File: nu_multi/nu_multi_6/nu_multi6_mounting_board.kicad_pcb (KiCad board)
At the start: 2 copper layers, 70 x 18.2 mm, 8 parts, among them J13 CONN_01X14, U1 nu_capsule, U2 nu_capsule, U3 nu_capsule, U4 nu_capsule, U5 nu_capsule, U6 nu_capsule

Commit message: Use 1x7p connector from cycfi lib
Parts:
- J13: footprint Pin_Headers:Pin_Header_Straight_2x07_Pitch1.00mm_SMD -> cycfi_library:pin_header_2x7p_1.00mm_smd_vertical

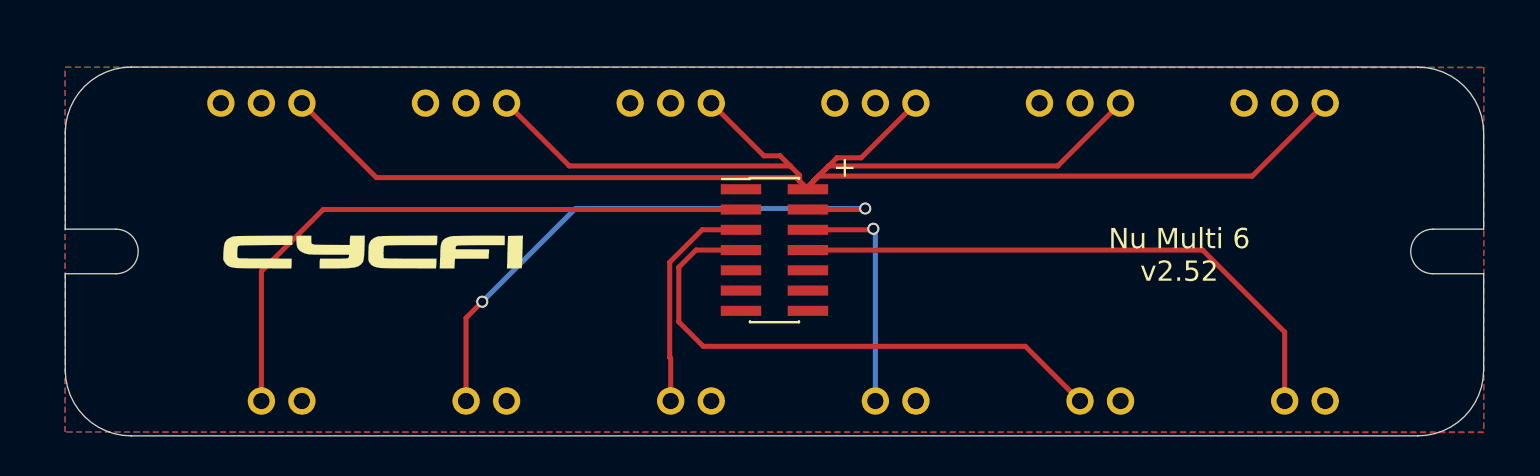
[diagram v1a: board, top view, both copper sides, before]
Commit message: - Upgrade to Kicad 8 - Update board to v2.53, minor edits,
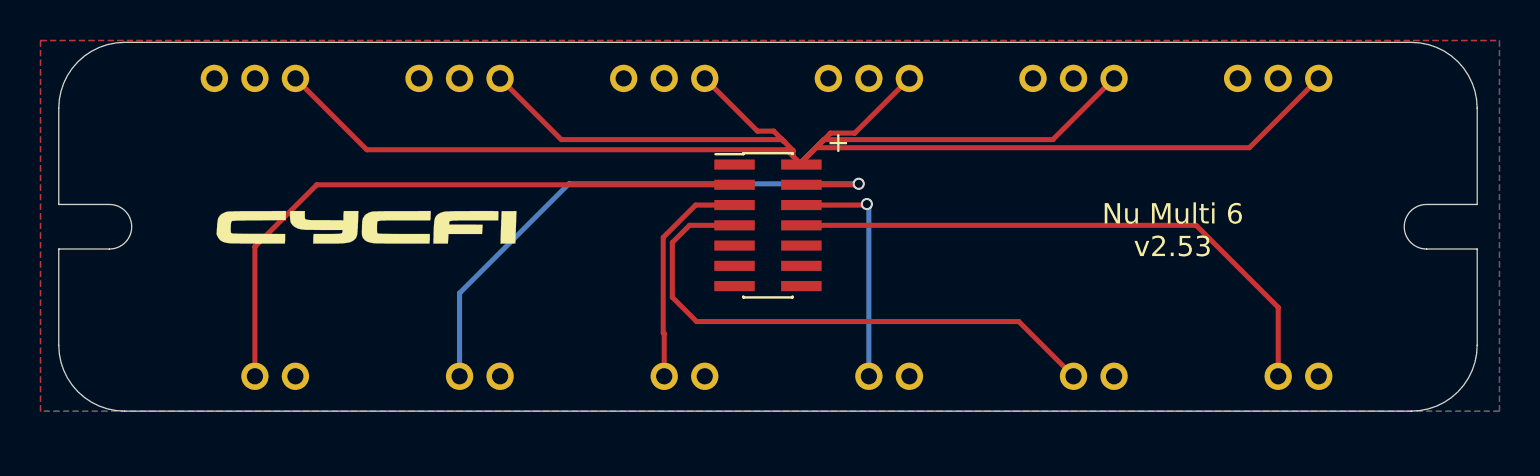
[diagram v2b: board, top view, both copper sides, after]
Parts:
- moved U4 1.26 mm to (142.0, 83.8)
- moved G*** 1.26 mm to (119.1, 91.2)
- moved J13 1.26 mm to (139.0, 91.0)
- moved U1 1.26 mm to (111.7, 83.8)
- moved U2 1.26 mm to (121.8, 83.8)
- moved U3 1.26 mm to (131.9, 83.8)
- moved U5 1.26 mm to (152.1, 83.8)
- moved U6 1.26 mm to (162.2, 83.8)
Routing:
- net CH2: vias 2 -> 1
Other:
- board text added: "Nu Multi 6 v2.53"
- board text removed: "Nu Multi 6 v2.52"

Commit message: Fixed string spacing! Bumped version to 2.54
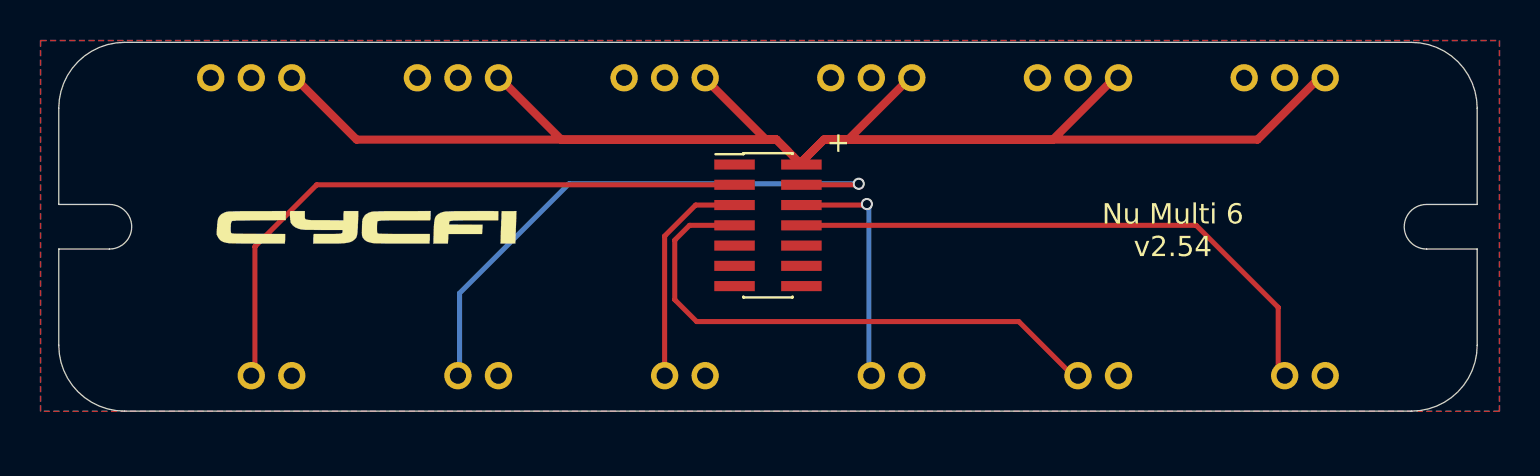
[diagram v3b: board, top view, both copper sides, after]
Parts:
- moved U6 0.32 mm to (162.5, 83.8)
- moved U5 0.22 mm to (152.3, 83.8)
- moved U1 0.18 mm to (111.5, 83.8)
- moved U4 0.12 mm to (142.1, 83.8)
- moved U2 0.09 mm to (121.7, 83.8)
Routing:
- net V+: track 99.3 -> 98.2 mm
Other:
- board text added: "Nu Multi 6 v2.54"
- board text removed: "Nu Multi 6 v2.53"
